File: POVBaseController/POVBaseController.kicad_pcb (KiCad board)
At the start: 2 copper layers, 50 x 23 mm, 58 parts, among them CON1 BARREL_JACK, P1 CONN_01X02, P2 CONN_01X02, P3 CONN_01X05, U1 DRV8848, U2 LM317AEMP, U3 CY8C4024LQI-S401

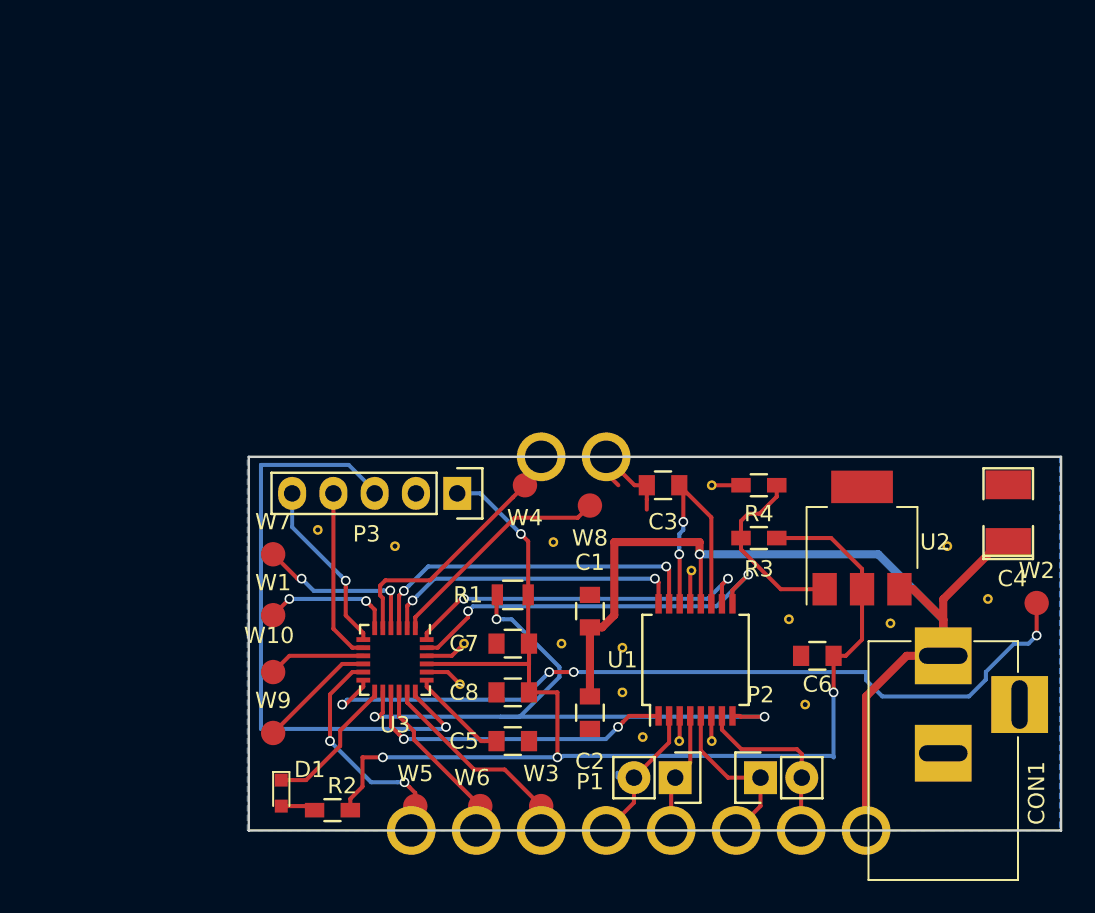
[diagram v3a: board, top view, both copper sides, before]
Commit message: Totally refactored the POV Base Controller.
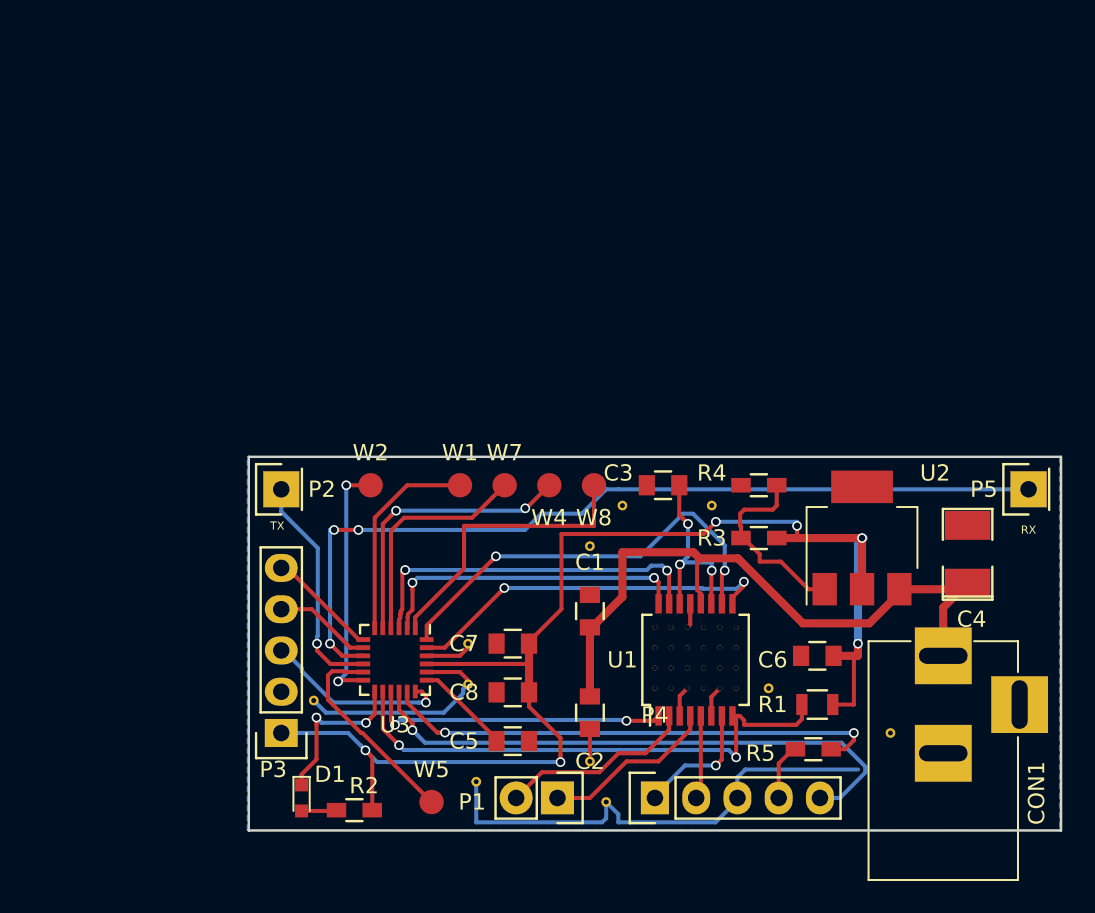
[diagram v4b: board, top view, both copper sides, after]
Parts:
- removed the REF** at (170.5, 105.8)
- removed the REF** at (153.5, 114.5)
- removed the REF** at (151.5, 114.5)
- removed the REF** at (152.2, 104.0)
- removed the REF** at (129.2, 101.5)
- removed the REF** at (138.0, 111.0)
- removed the REF** at (148.0, 108.8)
- removed the REF** at (144.2, 108.5)
- removed the REF** at (134.0, 102.5)
- removed the REF** at (163.0, 120.0)
- removed the REF** at (147.0, 97.0)
- removed the REF** at (168.0, 102.5)
- removed the REF** at (143.0, 97.0)
- removed the REF** at (135.0, 120.0)
- removed the REF** at (139.0, 120.0)
- removed the REF** at (143.0, 120.0)
- removed the REF** at (159.0, 120.0)
- removed the REF** at (155.0, 120.0)
- removed the REF** at (151.0, 120.0)
- removed the REF** at (147.0, 120.0)
- removed the REF** at (143.8, 102.2)
- removed the REF** at (164.5, 107.2)
- removed the REF** at (159.2, 112.2)
- removed the REF** at (158.2, 107.0)
- removed the REF** at (153.5, 98.8)
- removed the REF** at (138.2, 108.5)
- removed the REF** at (148.0, 111.5)
- removed the REF** at (149.2, 114.2)
- removed W10: RX, Measurement_Points:Measurement_Point_Round-SMD-Pad_Small
- removed W3, W6: TEST_1P, Measurement_Points:Measurement_Point_Round-SMD-Pad_Small
- removed W9: TX, Measurement_Points:Measurement_Point_Round-SMD-Pad_Small
- added P4: CONN_01X05, Socket_Strips:Socket_Strip_Straight_1x05, F.Cu at (150.0, 118.0)
- added P5: CONN_01X01, Socket_Strips:Socket_Strip_Straight_1x01, F.Cu at (173.0, 99.0)
- added R5: 1.5k, Resistors_SMD:R_0603_HandSoldering, F.Cu at (159.8, 115.0)
- added REF**: via_0.3mm, KicadFootprint:via_0.3mm, F.Cu at (146.0, 102.5)
- added REF**: via_0.3mm, KicadFootprint:via_0.3mm, F.Cu at (157.0, 111.2)
- added REF**: via_0.3mm, KicadFootprint:via_0.3mm, F.Cu at (155.0, 111.2)
- added REF**: via_0.3mm, KicadFootprint:via_0.3mm, F.Cu at (154.0, 111.2)
- added REF**: via_0.3mm, KicadFootprint:via_0.3mm, F.Cu at (153.0, 111.2)
- added REF**: via_0.3mm, KicadFootprint:via_0.3mm, F.Cu at (152.0, 111.2)
- added REF**: via_0.3mm, KicadFootprint:via_0.3mm, F.Cu at (151.0, 111.2)
- added REF**: via_0.3mm, KicadFootprint:via_0.3mm, F.Cu at (150.0, 111.2)
- added REF**: via_0.3mm, KicadFootprint:via_0.3mm, F.Cu at (150.0, 110.0)
- added REF**: via_0.3mm, KicadFootprint:via_0.3mm, F.Cu at (151.0, 110.0)
- added REF**: via_0.3mm, KicadFootprint:via_0.3mm, F.Cu at (152.0, 110.0)
- added REF**: via_0.3mm, KicadFootprint:via_0.3mm, F.Cu at (147.0, 118.2)
- added REF**: via_0.3mm, KicadFootprint:via_0.3mm, F.Cu at (153.0, 110.0)
- added REF**: via_0.3mm, KicadFootprint:via_0.3mm, F.Cu at (154.0, 110.0)
- added REF**: via_0.3mm, KicadFootprint:via_0.3mm, F.Cu at (155.0, 110.0)
- added REF**: via_0.3mm, KicadFootprint:via_0.3mm, F.Cu at (150.0, 108.8)
- added REF**: via_0.3mm, KicadFootprint:via_0.3mm, F.Cu at (151.0, 108.8)
- added REF**: via_0.3mm, KicadFootprint:via_0.3mm, F.Cu at (152.0, 108.8)
- added REF**: via_0.3mm, KicadFootprint:via_0.3mm, F.Cu at (153.0, 108.8)
- added REF**: via_0.3mm, KicadFootprint:via_0.3mm, F.Cu at (154.0, 108.8)
- added REF**: via_0.3mm, KicadFootprint:via_0.3mm, F.Cu at (155.0, 108.8)
- added REF**: via_0.3mm, KicadFootprint:via_0.3mm, F.Cu at (155.0, 107.5)
- added REF**: via_0.3mm, KicadFootprint:via_0.3mm, F.Cu at (146.0, 115.8)
- added REF**: via_0.3mm, KicadFootprint:via_0.3mm, F.Cu at (154.0, 107.5)
- added REF**: via_0.3mm, KicadFootprint:via_0.3mm, F.Cu at (153.0, 107.5)
- added REF**: via_0.3mm, KicadFootprint:via_0.3mm, F.Cu at (152.0, 107.5)
- added REF**: via_0.3mm, KicadFootprint:via_0.3mm, F.Cu at (151.0, 107.5)
- added REF**: via_0.3mm, KicadFootprint:via_0.3mm, F.Cu at (150.0, 107.5)
- added REF**: via_0.3mm, KicadFootprint:via_0.3mm, F.Cu at (164.5, 114.0)
- added REF**: via_0.3mm, KicadFootprint:via_0.3mm, F.Cu at (153.5, 100.0)
- added REF**: via_0.3mm, KicadFootprint:via_0.3mm, F.Cu at (148.0, 100.0)
- added REF**: via_0.3mm, KicadFootprint:via_0.3mm, F.Cu at (129.0, 112.0)
- added REF**: via_0.3mm, KicadFootprint:via_0.3mm, F.Cu at (139.0, 117.0)
- added REF**: via_0.3mm, KicadFootprint:via_0.3mm, F.Cu at (138.5, 108.5)
- added REF**: via_0.3mm, KicadFootprint:via_0.3mm, F.Cu at (138.5, 111.0)
- P2: value CONN_01X02 -> CONN_01X01; footprint Socket_Strips:Socket_Strip_Straight_1x02 -> Socket_Strips:Socket_Strip_Straight_1x01
- moved W2 41.6 mm to (132.5, 98.8)
- moved P2 34.4 mm to (127.0, 99.0)
- moved R1 19.9 mm to (160.0, 112.2)
- moved P3 18.3 mm to (127.0, 114.0), turned to 90 degrees
- moved W7 14.9 mm to (140.8, 98.8)
- moved W1 14.0 mm to (138.0, 98.8)
- moved P1 7.36 mm to (144.0, 118.0)
- moved C4 3.54 mm to (169.2, 103.0)
- moved W4 1.50 mm to (143.5, 98.8)
- moved R2 1.35 mm to (131.5, 118.8)
- moved D1 1.29 mm to (128.2, 118.0)
- moved W8 1.27 mm to (146.2, 98.8)
- moved W5 1.03 mm to (136.2, 118.2)
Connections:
- P2 pad 1: /MOTOR_OUT_B -> /UART_TX
- U3 pad 16: Net-(U3-Pad16) -> /SPARE
- U3 pad 17: Net-(U3-Pad17) -> /NIR_EMITTER_LS
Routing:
- net /UART_RX: track 5.96 -> 53.4 mm, vias 0 -> 3
- net /SPARE: track 0.00 -> 35.3 mm, vias 0 -> 1
- net Net-(U3-Pad12): track 50.5 -> 15.4 mm, vias 4 -> 2
- net GND: track 18.8 -> 53.6 mm
- net /NIR_EMITTER_LS: track 0.00 -> 31.0 mm, vias 0 -> 2
- net /XRES: track 38.5 -> 11.5 mm
- net +12V: track 67.2 -> 42.1 mm, vias 1 -> 0
- net Net-(U3-Pad17): track 12.6 -> 0.00 mm
- net Net-(U3-Pad16): track 10.3 -> 0.00 mm
- net /UART_TX: track 7.31 -> 14.1 mm, vias 0 -> 1
- net /nFAULT: track 39.8 -> 33.1 mm, vias 3 -> 2
- net /MOTOR_OUT_B: track 10.4 -> 5.17 mm
- net Net-(U3-Pad6): track 8.08 -> 12.9 mm, vias 2 -> 0
- net /SWDCLK: track 10.7 -> 6.03 mm
- net /MOTOR_IN_B: track 22.0 -> 26.5 mm
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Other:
- board text added: "RX"
- board text added: "TX"

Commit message: Ordered the POV Base Controller and the POV Base Coil.
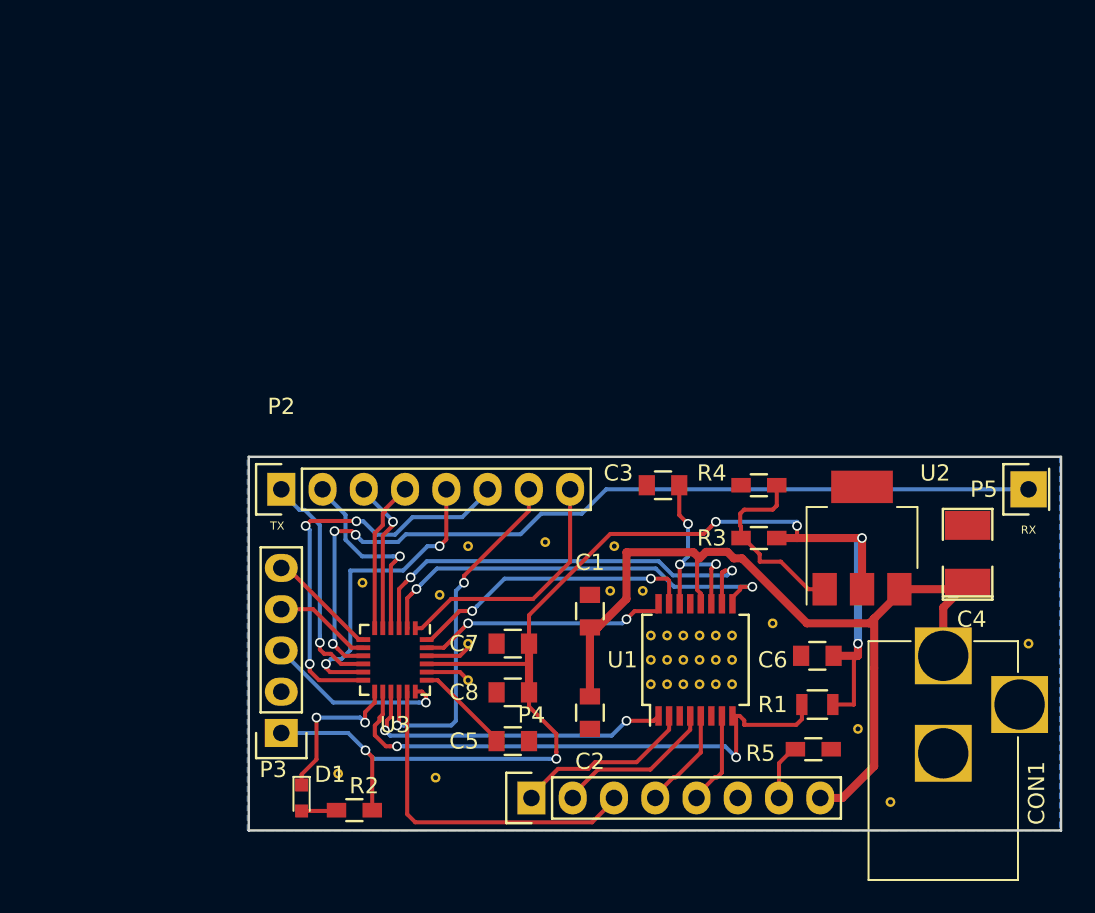
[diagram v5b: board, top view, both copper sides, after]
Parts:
- removed P1: CONN_01X02, Socket_Strips:Socket_Strip_Straight_1x02
- removed the REF** at (146.0, 102.5)
- removed the REF** at (157.0, 111.2)
- removed the REF** at (155.0, 111.2)
- removed the REF** at (154.0, 111.2)
- removed the REF** at (153.0, 111.2)
- removed the REF** at (152.0, 111.2)
- removed the REF** at (151.0, 111.2)
- removed the REF** at (150.0, 111.2)
- removed the REF** at (150.0, 110.0)
- removed the REF** at (151.0, 110.0)
- removed the REF** at (152.0, 110.0)
- removed the REF** at (147.0, 118.2)
- removed the REF** at (153.0, 110.0)
- removed the REF** at (154.0, 110.0)
- removed the REF** at (155.0, 110.0)
- removed the REF** at (150.0, 108.8)
- removed the REF** at (151.0, 108.8)
- removed the REF** at (152.0, 108.8)
- removed the REF** at (153.0, 108.8)
- removed the REF** at (154.0, 108.8)
- removed the REF** at (155.0, 108.8)
- removed the REF** at (155.0, 107.5)
- removed the REF** at (146.0, 115.8)
- removed the REF** at (154.0, 107.5)
- removed the REF** at (153.0, 107.5)
- removed the REF** at (152.0, 107.5)
- removed the REF** at (151.0, 107.5)
- removed the REF** at (150.0, 107.5)
- removed the REF** at (164.5, 114.0)
- removed the REF** at (153.5, 100.0)
- removed the REF** at (148.0, 100.0)
- removed the REF** at (129.0, 112.0)
- removed the REF** at (139.0, 117.0)
- removed the REF** at (138.5, 111.0)
- removed W1, W2, W4, W5, W7, W8: TEST_1P, Measurement_Points:Measurement_Point_Round-SMD-Pad_Small
- added REF**: via_0.3mm, KicadFootprint:via_0.3mm, F.Cu at (138.5, 110.8)
- added REF**: via_0.3mm, KicadFootprint:via_0.3mm, F.Cu at (147.2, 105.2)
- added REF**: via_0.3mm, KicadFootprint:via_0.3mm, F.Cu at (149.2, 105.2)
- added REF**: via_0.3mm, KicadFootprint:via_0.3mm, F.Cu at (149.8, 111.0)
- added REF**: via_0.3mm, KicadFootprint:via_0.3mm, F.Cu at (150.8, 111.0)
- added REF**: via_0.3mm, KicadFootprint:via_0.3mm, F.Cu at (151.8, 111.0)
- added REF**: via_0.3mm, KicadFootprint:via_0.3mm, F.Cu at (152.8, 111.0)
- added REF**: via_0.3mm, KicadFootprint:via_0.3mm, F.Cu at (153.8, 111.0)
- added REF**: via_0.3mm, KicadFootprint:via_0.3mm, F.Cu at (154.8, 111.0)
- added REF**: via_0.3mm, KicadFootprint:via_0.3mm, F.Cu at (154.8, 109.5)
- added REF**: via_0.3mm, KicadFootprint:via_0.3mm, F.Cu at (153.8, 109.5)
- added REF**: via_0.3mm, KicadFootprint:via_0.3mm, F.Cu at (152.8, 109.5)
- added REF**: via_0.3mm, KicadFootprint:via_0.3mm, F.Cu at (151.8, 109.5)
- added REF**: via_0.3mm, KicadFootprint:via_0.3mm, F.Cu at (150.8, 109.5)
- added REF**: via_0.3mm, KicadFootprint:via_0.3mm, F.Cu at (149.8, 109.5)
- added REF**: via_0.3mm, KicadFootprint:via_0.3mm, F.Cu at (149.8, 108.0)
- added REF**: via_0.3mm, KicadFootprint:via_0.3mm, F.Cu at (150.8, 108.0)
- added REF**: via_0.3mm, KicadFootprint:via_0.3mm, F.Cu at (151.8, 108.0)
- added REF**: via_0.3mm, KicadFootprint:via_0.3mm, F.Cu at (152.8, 108.0)
- added REF**: via_0.3mm, KicadFootprint:via_0.3mm, F.Cu at (153.8, 108.0)
- added REF**: via_0.3mm, KicadFootprint:via_0.3mm, F.Cu at (154.8, 108.0)
- added REF**: via_0.3mm, KicadFootprint:via_0.3mm, F.Cu at (136.5, 116.8)
- added REF**: via_0.3mm, KicadFootprint:via_0.3mm, F.Cu at (157.2, 107.2)
- added REF**: via_0.3mm, KicadFootprint:via_0.3mm, F.Cu at (162.5, 113.8)
- added REF**: via_0.3mm, KicadFootprint:via_0.3mm, F.Cu at (164.5, 118.2)
- added REF**: via_0.3mm, KicadFootprint:via_0.3mm, F.Cu at (173.0, 108.5)
- added REF**: via_0.3mm, KicadFootprint:via_0.3mm, F.Cu at (130.5, 116.5)
- added REF**: via_0.3mm, KicadFootprint:via_0.3mm, F.Cu at (132.0, 104.8)
- added REF**: via_0.3mm, KicadFootprint:via_0.3mm, F.Cu at (136.8, 105.5)
- added REF**: via_0.3mm, KicadFootprint:via_0.3mm, F.Cu at (138.5, 102.5)
- added REF**: via_0.3mm, KicadFootprint:via_0.3mm, F.Cu at (143.2, 102.2)
- added REF**: via_0.3mm, KicadFootprint:via_0.3mm, F.Cu at (147.5, 102.5)
- P2: value CONN_01X01 -> CONN_01X08; footprint Socket_Strips:Socket_Strip_Straight_1x01 -> Socket_Strips:Socket_Strip_Straight_1x08
- P4: value CONN_01X05 -> CONN_01X08; footprint Socket_Strips:Socket_Strip_Straight_1x05 -> Socket_Strips:Socket_Strip_Straight_1x08
- moved P4 7.60 mm to (142.4, 118.0)
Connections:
- P4 pad 3: GND -> /SPARE_8
- P4 pad 4: /NIR_EMITTER -> /COIL_OUT_B
- P4 pad 5: /SPARE -> /COIL_OUT_A
- R5 pad 2: /NIR_EMITTER_LS -> GND
- U1 pad 10: /MOTOR_IN_B -> /COIL_IN_B
- U1 pad 15: /COIL_IN_B -> /MOTOR_IN_B
- U1 pad 16: /COIL_IN_A -> /MOTOR_IN_A
- U1 pad 2: /COIL_OUT_A -> /MOTOR_OUT_A
- U1 pad 4: /COIL_OUT_B -> /MOTOR_OUT_B
- U1 pad 5: /MOTOR_OUT_B -> /COIL_OUT_B
- U1 pad 7: /MOTOR_OUT_A -> /COIL_OUT_A
- U1 pad 9: /MOTOR_IN_A -> /COIL_IN_A
- U3 pad 1: Net-(U3-Pad1) -> /SPARE_7
- U3 pad 11: Net-(U3-Pad11) -> /SPARE_4
- U3 pad 12: Net-(U3-Pad12) -> /SPARE_5
- U3 pad 16: /SPARE -> /SPARE_6
- U3 pad 17: /NIR_EMITTER_LS -> /SPARE_8
- U3 pad 4: Net-(U3-Pad4) -> /SPARE_1
- U3 pad 5: Net-(U3-Pad5) -> /SPARE_2
- U3 pad 6: Net-(U3-Pad6) -> /SPARE_3
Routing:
- net GND: track 53.6 -> 5.51 mm
- net /SPARE: track 35.3 -> 0.00 mm, vias 1 -> 0
- net /NIR_EMITTER_LS: track 31.0 -> 0.00 mm, vias 2 -> 0
- net /SPARE_5: track 0.00 -> 25.5 mm, vias 0 -> 3
- net /SPARE_6: track 0.00 -> 22.0 mm, vias 0 -> 2
- net /SPARE_8: track 0.00 -> 21.2 mm
- net /SPARE_4: track 0.00 -> 19.2 mm, vias 0 -> 2
- net Net-(U3-Pad1): track 18.0 -> 0.00 mm
- net Net-(U3-Pad5): track 17.7 -> 0.00 mm, vias 2 -> 0
- net /SPARE_7: track 0.00 -> 15.7 mm
- net Net-(U3-Pad12): track 15.4 -> 0.00 mm, vias 2 -> 0
- net Net-(U3-Pad4): track 14.2 -> 0.00 mm
- net +12V: track 42.1 -> 55.7 mm
- net Net-(U3-Pad6): track 12.9 -> 0.00 mm
- net Net-(U3-Pad11): track 12.8 -> 0.00 mm
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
